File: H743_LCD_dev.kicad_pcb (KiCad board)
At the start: 2 copper layers, 39 parts, among them J1 BAT_SW, J2 TFT_LCD, J3 CAPACITIVE_CONTROLLER, SW1 SW_Push, U1 IS42S32800J-6TL, U2 STM32H743IITx

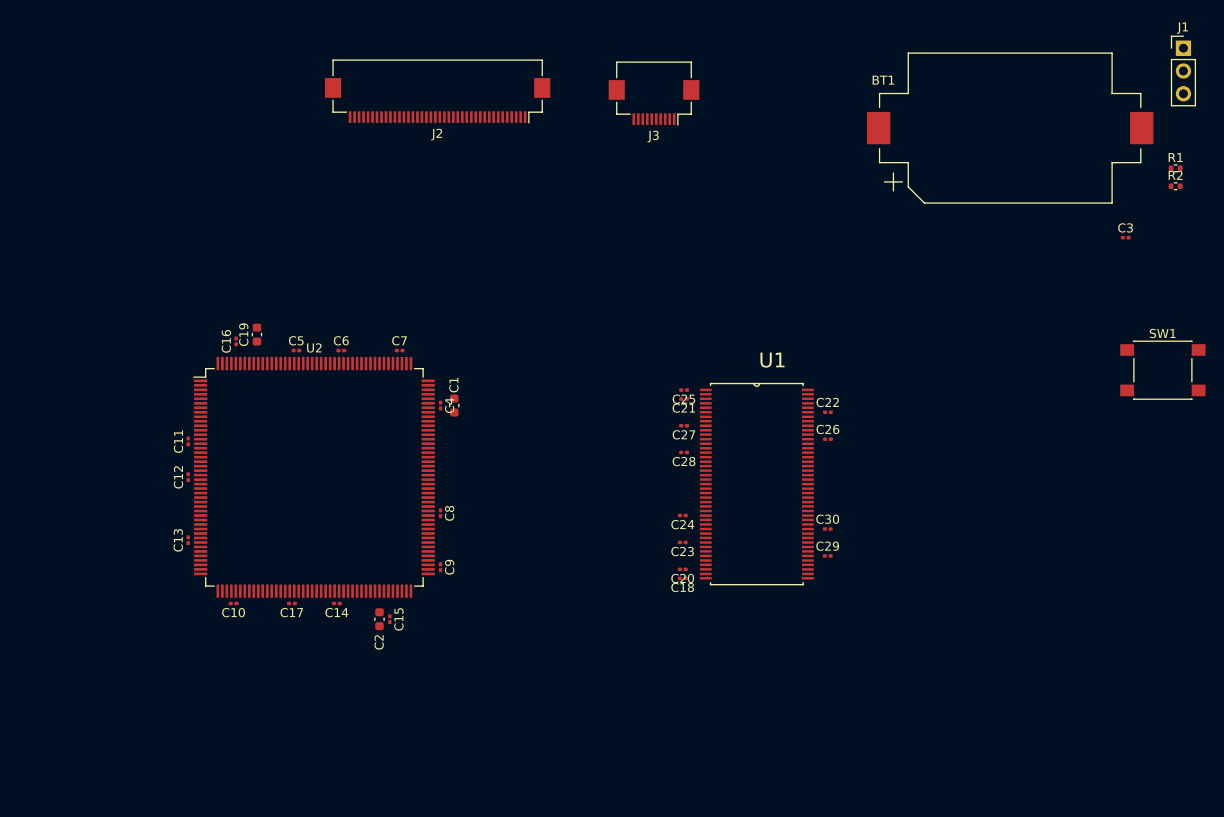
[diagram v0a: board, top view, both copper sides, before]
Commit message: Added UART, i2c, debug, NAND Flash, NOR Flash, EEPROM, SD-Card
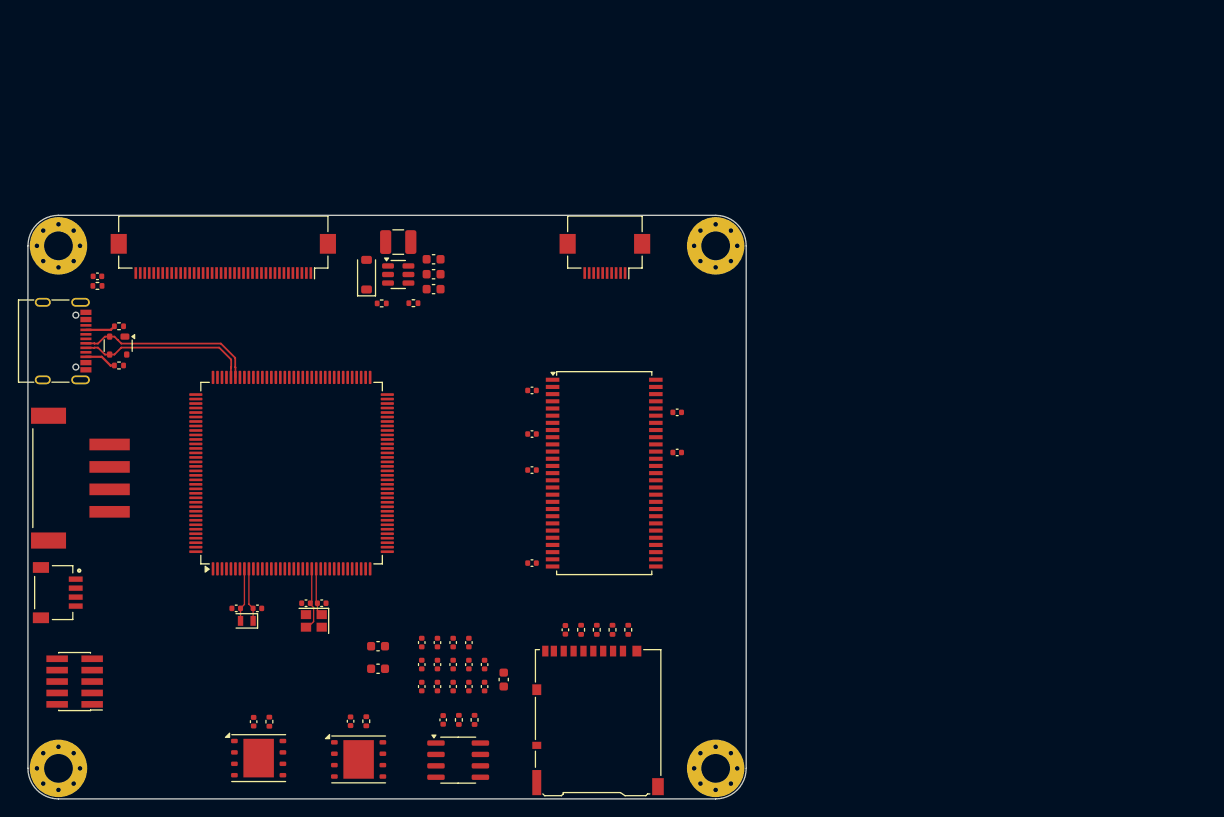
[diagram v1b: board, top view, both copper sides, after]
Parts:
- removed BT1: Battery_Cell, Battery:BatteryHolder_Keystone_1060_1x2032
- removed C23, C24, C25, C26, C27, C28, C29, C30: 100n, Capacitor_SMD:C_0201_0603Metric
- removed SW1: SW_Push, Button_Switch_SMD:SW_SPST_PTS645
- added C31: 1u, Capacitor_SMD:C_0603_1608Metric, F.Cu at (147.5, 74.8)
- added C32: 10u, Capacitor_SMD:C_0603_1608Metric, F.Cu at (147.5, 76.4)
- added C33: 10u, Capacitor_SMD:C_0603_1608Metric, F.Cu at (147.5, 78.1)
- added C34: 2u2, Capacitor_SMD:C_0603_1608Metric, F.Cu at (141.4, 117.9)
- added C35: 2u2, Capacitor_SMD:C_0603_1608Metric, F.Cu at (141.4, 120.4)
- added C36: 100n, Capacitor_SMD:C_0402_1005Metric, F.Cu at (158.5, 89.4)
- added C37: 100n, Capacitor_SMD:C_0402_1005Metric, F.Cu at (174.7, 96.3)
- added C38: 100n, Capacitor_SMD:C_0402_1005Metric, F.Cu at (174.7, 91.8)
- added C39: 10p, Capacitor_SMD:C_0402_1005Metric, F.Cu at (133.3, 113.1)
- added C40: 10p, Capacitor_SMD:C_0402_1005Metric, F.Cu at (135.1, 113.1)
- added C41: 22p, Capacitor_SMD:C_0402_1005Metric, F.Cu at (127.9, 113.7)
- added C42: 22p, Capacitor_SMD:C_0402_1005Metric, F.Cu at (125.6, 113.7)
- added C43: 4n7, Capacitor_SMD:C_0402_1005Metric, F.Cu at (110.1, 76.7)
- added D1: MSK4010, Diode_SMD:D_SOD-123, F.Cu at (140.1, 76.5)
- added D2: PRTR5V0U2X, Package_TO_SOT_SMD:SOT-143, F.Cu at (112.4, 84.4)
- added H1: MountingHole_Pad, MountingHole:MountingHole_3.2mm_M3_Pad_Via, F.Cu at (179.0, 131.5)
- added H2: MountingHole_Pad, MountingHole:MountingHole_3.2mm_M3_Pad_Via, F.Cu at (105.8, 131.5)
- added H3: MountingHole_Pad, MountingHole:MountingHole_3.2mm_M3_Pad_Via, F.Cu at (105.8, 73.3)
- added H4: MountingHole_Pad, MountingHole:MountingHole_3.2mm_M3_Pad_Via, F.Cu at (179.0, 73.3)
- added J4: USB-C, Connector_USB:USB_C_Receptacle_G-Switch_GT-USB-7010ASV, F.Cu at (105.1, 83.9)
- added J5: I2C-STEMMA-QT, SM04B-SRSS-TB_LF__SN_:JST_SM04B-SRSS-TB_LF__SN_, F.Cu at (107.7, 111.9)
- added J6: UART, KiCad:S4BXHSM4TBLFSN, F.Cu at (107.2, 99.2)
- added J7: Conn_02x05_Odd_Even, Connector_PinHeader_1.27mm:PinHeader_2x05_P1.27mm_Vertical_SMD, F.Cu at (107.6, 121.8)
- added L1: 10uH, Inductor_SMD:L_1210_3225Metric, F.Cu at (143.6, 72.9)
- added R10: 10K, Resistor_SMD:R_0402_1005Metric, F.Cu at (169.2, 116.1)
- added R11: 5K1, Resistor_SMD:R_0402_1005Metric, F.Cu at (112.5, 82.2)
- added R12: 5K1, Resistor_SMD:R_0402_1005Metric, F.Cu at (112.5, 86.6)
- added R13: 1M, Resistor_SMD:R_0402_1005Metric, F.Cu at (110.1, 77.7)
- added R3: 2.74R, Resistor_SMD:R_0402_1005Metric, F.Cu at (141.8, 79.7)
- added R4: 5K1, Resistor_SMD:R_0402_1005Metric, F.Cu at (145.3, 79.7)
- added R5: 2K2, Resistor_SMD:R_0402_1005Metric, F.Cu at (150.4, 126.1)
- added R6: 2K2, Resistor_SMD:R_0402_1005Metric, F.Cu at (152.1, 126.1)
- added R7: 10K, Resistor_SMD:R_0402_1005Metric, F.Cu at (164.0, 116.1)
- added R8: 10K, Resistor_SMD:R_0402_1005Metric, F.Cu at (165.7, 116.1)
- added R9: 10K, Resistor_SMD:R_0402_1005Metric, F.Cu at (167.5, 116.1)
- added U3: MT9284, Package_TO_SOT_SMD:SOT-23-6, F.Cu at (143.6, 76.5)
- added U4: STM32H723ZGTx, Package_QFP:LQFP-144_20x20mm_P0.5mm, F.Cu at (131.7, 98.6)
- added U5: W25N01GVZEIG, Package_SON:WSON-8-1EP_6x5mm_P1.27mm_EP3.4x4.3mm, F.Cu at (139.2, 130.5)
- added U7: CAT24C128, Package_SO:SOIC-8_3.9x4.9mm_P1.27mm, F.Cu at (150.3, 130.6)
- added Y1: 25MHz, Crystal:Crystal_SMD_2520-4Pin_2.5x2.0mm, F.Cu at (134.2, 115.1)
- added Y2: 32.768KHz, Crystal:Crystal_SMD_2012-2Pin_2.0x1.2mm, F.Cu at (126.7, 115.1)
- C1, C2: value 2u2 -> 100n; footprint Capacitor_SMD:C_0603_1608Metric -> Capacitor_SMD:C_0402_1005Metric
- C10, C11, C12, C13, C14, C15, C16, C17, C18, C20, C21, C22, C3, C4, C5, C6, C7, C8, C9: footprint Capacitor_SMD:C_0201_0603Metric -> Capacitor_SMD:C_0402_1005Metric
- J1: value BAT_SW -> Micro_SD_Card_Det_Hirose_DM3AT; footprint Connector_PinHeader_2.54mm:PinHeader_1x03_P2.54mm_Vertical -> Connector_Card:microSD_HC_Hirose_DM3AT-SF-PEJM5
- U1: value IS42S32800J-6TL -> W25Q128JVS; footprint IS42S32800J-6TL:SOP50P1176X120-86N -> Package_SON:WSON-8-1EP_6x5mm_P1.27mm_EP3.4x4.3mm
- U2: value STM32H743IITx -> IS42S16160J-7TL; footprint Package_QFP:LQFP-176_24x24mm_P0.5mm -> Package_SO:TSOP-II-54_22.2x10.16mm_P0.8mm
- moved R2 117.2 mm to (129.3, 126.3), turned to 90 degrees
- moved R1 109.2 mm to (140.1, 126.2), turned to 90 degrees
- moved J1 99.3 mm to (165.9, 126.1)
- moved C3 69.6 mm to (158.5, 94.2), turned to 180 degrees
- moved C22 63.3 mm to (138.3, 126.2), turned to 90 degrees
- moved U1 63.3 mm to (128.1, 130.3)
- moved C21 59.9 mm to (127.5, 126.3), turned to 90 degrees
- moved C19 47.2 mm to (155.4, 121.6)
- moved C16 41.4 mm to (149.7, 117.5)
- moved C5 40.6 mm to (148.0, 122.4), turned to 90 degrees
- moved C6 39.4 mm to (149.7, 122.4), turned to 90 degrees
- moved C11 38.6 mm to (149.7, 119.9)
- moved C7 38.2 mm to (151.5, 122.4), turned to 90 degrees
- moved C12 37.6 mm to (151.5, 119.9)
- moved C13 35.8 mm to (153.2, 119.9), turned to 90 degrees
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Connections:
- net /MEMORY/D0 renamed /MEMORY/NOR_DO(IO1)
- net /MEMORY/D2 renamed /MEMORY/NOR_DI(IO0)
- net /MEMORY/D3 renamed /MEMORY/NOR_IO3
- C1 pad 1: Net-(C1-Pad1) -> +3V3
- C10 pad 1: VDD -> +3V3
- C11 pad 1: VDD -> +3V3
- C12 pad 1: VDD -> +3V3
- C13 pad 1: VDD -> +3V3
- C14 pad 1: VDD -> +3V3
- C15 pad 1: VDD -> +3V3
- C16 pad 1: VDD -> +3V3
- C17 pad 1: VDD -> +3V3
- C19 pad 1: VDD -> +3V3
- C2 pad 1: Net-(C2-Pad1) -> +3V3
- C3 pad 1: GND -> +3V3
- C3 pad 2: /MCU/RST -> GND
- C4 pad 1: VDD -> +3V3
- C5 pad 1: VDD -> +3V3
- C6 pad 1: VDD -> +3V3
- C7 pad 1: VDD -> +3V3
- C8 pad 1: VDD -> +3V3
- C9 pad 1: VDD -> +3V3
- J1 pad 1: +3V3 -> /MEMORY/SD_DAT2
- J1 pad 2: Net-(J1-Pin_2) -> /MEMORY/SD_DAT3/CD
- J1 pad 3: Net-(BT1-+) -> /MEMORY/SD_CMD
- J2 pad 1: unconnected-(J2-Pad1) -> /LCD/LED_K
- J2 pad 10: unconnected-(J2-Pad10) -> /LCD/LCD_R5
- J2 pad 11: unconnected-(J2-Pad11) -> /LCD/LCD_R6
- J2 pad 12: unconnected-(J2-Pad12) -> /LCD/LCD_R7
- J2 pad 13: unconnected-(J2-Pad13) -> /LCD/LCD_G0
- J2 pad 14: unconnected-(J2-Pad14) -> /LCD/LCD_G1
- J2 pad 15: unconnected-(J2-Pad15) -> /LCD/LCD_G2
- J2 pad 16: unconnected-(J2-Pad16) -> /LCD/LCD_G3
- J2 pad 17: unconnected-(J2-Pad17) -> /LCD/LCD_G4
- J2 pad 18: unconnected-(J2-Pad18) -> /LCD/LCD_G5
- J2 pad 19: unconnected-(J2-Pad19) -> /LCD/LCD_G6
- J2 pad 2: unconnected-(J2-Pad2) -> /LCD/LED_A
- J2 pad 20: unconnected-(J2-Pad20) -> /LCD/LCD_G7
- J2 pad 21: unconnected-(J2-Pad21) -> /LCD/LCD_B0
- J2 pad 22: unconnected-(J2-Pad22) -> /LCD/LCD_B1
- J2 pad 23: unconnected-(J2-Pad23) -> /LCD/LCD_B2
- J2 pad 24: unconnected-(J2-Pad24) -> /LCD/LCD_B3
- J2 pad 25: unconnected-(J2-Pad25) -> /LCD/LCD_B4
- J2 pad 26: unconnected-(J2-Pad26) -> /LCD/LCD_B5
- J2 pad 27: unconnected-(J2-Pad27) -> /LCD/LCD_B6
- J2 pad 28: unconnected-(J2-Pad28) -> /LCD/LCD_B7
- J2 pad 29: unconnected-(J2-Pad29) -> GND
- J2 pad 30: unconnected-(J2-Pad30) -> /LCD/LCD_CLK
- J2 pad 31: unconnected-(J2-Pad31) -> /LCD/LCD_DISP
- J2 pad 32: unconnected-(J2-Pad32) -> /LCD/HSYNC
- J2 pad 33: unconnected-(J2-Pad33) -> /LCD/VSYNC
- J2 pad 34: unconnected-(J2-Pad34) -> /LCD/LCD_DE
- J2 pad 36: unconnected-(J2-Pad36) -> GND
- J2 pad 37: unconnected-(J2-Pad37) -> /LCD/XR
- J2 pad 38: unconnected-(J2-Pad38) -> /LCD/YD
- J2 pad 39: unconnected-(J2-Pad39) -> /LCD/XL
- J2 pad 4: unconnected-(J2-Pad4) -> VDD
- J2 pad 40: unconnected-(J2-Pad40) -> /LCD/YU
- J2 pad 5: unconnected-(J2-Pad5) -> /LCD/LCD_R0
- J2 pad 6: unconnected-(J2-Pad6) -> /LCD/LCD_R1
- J2 pad 7: unconnected-(J2-Pad7) -> /LCD/LCD_R2
- J2 pad 8: unconnected-(J2-Pad8) -> /LCD/LCD_R3
- J2 pad 9: unconnected-(J2-Pad9) -> /LCD/LCD_R4
- J2 pad MP: unconnected-(J2-MOUNT-PadMP) -> GND
- J3 pad 1: unconnected-(J3-Pad1) -> GND
- J3 pad 10: unconnected-(J3-Pad10) -> GND
- J3 pad 2: unconnected-(J3-Pad2) -> VDD
- J3 pad 3: unconnected-(J3-Pad3) -> /LCD/LCD_SCL
- J3 pad 4: unconnected-(J3-Pad4) -> GND
- J3 pad 5: unconnected-(J3-Pad5) -> /LCD/LCD_SDA
- J3 pad 6: unconnected-(J3-Pad6) -> GND
- J3 pad 7: unconnected-(J3-Pad7) -> /LCD/~{LCD_RST}
- J3 pad 8: unconnected-(J3-Pad8) -> /LCD/LCD_WAKE
- J3 pad 9: unconnected-(J3-Pad9) -> /LCD/~{LCD_INT}
- J3 pad MP: unconnected-(J3-MOUNT-PadMP) -> GND
- R1 pad 1: VDD -> +3V3
- R1 pad 2: Net-(U2-PDR_ON) -> /MEMORY/~{NAND_CS}
- R2 pad 1: VDD -> +3V3
- R2 pad 2: /MCU/RST -> /MEMORY/~{NOR_CS}
- U1 pad 1: +3V3 -> /MEMORY/~{NOR_CS}
- U1 pad 3: +3V3 -> /MEMORY/NOR_IO2
- U1 pad 4: /MEMORY/D1 -> GND
- U1 pad 6: GND -> /MEMORY/NOR_CLK
- U1 pad 8: /MEMORY/D4 -> +3V3
- U1 pad 9: +3V3 -> GND
- U2 pad 1: /MCU/PE2 -> +3V3
- U2 pad 10: /MCU/PC15 -> /MCU/DQ5
- U2 pad 11: /MCU/PI9 -> /MCU/DQ6
- U2 pad 12: /MCU/PI10 -> GND
- U2 pad 13: /MCU/PI11 -> /MCU/DQ7
- U2 pad 14: GND -> +3V3
- U2 pad 15: VDD -> /MCU/PE0
- U2 pad 16: /MCU/PF0 -> /MCU/PC0
- U2 pad 17: /MCU/PF1 -> /MCU/PG15
- U2 pad 18: /MCU/PF2 -> /MCU/PF11
- U2 pad 19: /MCU/PF3 -> /MCU/PC4
- U2 pad 2: /MCU/PE3 -> /MCU/DQ0
- U2 pad 20: /MCU/PF4 -> /MCU/PG4
- U2 pad 21: /MCU/PF5 -> /MCU/PG5
- U2 pad 22: GND -> /MCU/A10
- U2 pad 23: VDD -> /MCU/A0
- U2 pad 24: /MCU/PF6 -> /MCU/A1
- U2 pad 25: /MCU/PF7 -> /MCU/A2
- U2 pad 26: /MCU/PF8 -> /MCU/A3
- U2 pad 27: /MCU/PF9 -> +3V3
- U2 pad 28: /MCU/PF10 -> GND
- U2 pad 29: /MCU/PH0 -> /MCU/A4
- U2 pad 3: /MCU/PE4 -> +3V3
- U2 pad 30: /MCU/PH1 -> /MCU/A5
- U2 pad 31: /MCU/RST -> /MCU/A6
- U2 pad 32: /MCU/PC0 -> /MCU/A7
- U2 pad 33: /MCU/PC1 -> /MCU/A8
- U2 pad 34: /MCU/PC2 -> /MCU/A9
- U2 pad 35: /MCU/PC3 -> /MCU/A11
- U2 pad 36: VDD -> unconnected-(U2-NC-Pad36)
- U2 pad 37: GND -> /MCU/PC5
- U2 pad 38: unconnected-(U2-VREF+-Pad38) -> /MCU/PG8
- U2 pad 39: /MCU/VDDA -> /MCU/PE1
- U2 pad 4: /MCU/PE5 -> /MCU/DQ1
- U2 pad 40: /MCU/PA0 -> unconnected-(U2-NC-Pad40)
- U2 pad 41: /MCU/PA1 -> GND
- U2 pad 42: /MCU/PA2 -> /MCU/DQ8
- U2 pad 43: /MCU/PH2 -> +3V3
- U2 pad 44: /MCU/PH3 -> /MCU/DQ9
- U2 pad 45: /MCU/PH4 -> /MCU/DQ10
- U2 pad 46: /MCU/PH5 -> GND
- U2 pad 47: /MCU/PA3 -> /MCU/DQ11
- U2 pad 48: GND -> /MCU/DQ12
- U2 pad 49: VDD -> +3V3
- U2 pad 5: /MCU/PE6 -> /MCU/DQ2
- U2 pad 50: /MCU/PA4 -> /MCU/DQ13
- U2 pad 51: /MCU/PA5 -> /MCU/DQ14
- U2 pad 52: /MCU/PA6 -> GND
- U2 pad 53: /MCU/PA7 -> /MCU/DQ15
- U2 pad 54: /MCU/PC4 -> GND
- U2 pad 6: Net-(J1-Pin_2) -> GND
- U2 pad 7: /MCU/PI8 -> /MCU/DQ3
- U2 pad 8: /MCU/PC13 -> /MCU/DQ4
- U2 pad 9: /MCU/PC14 -> +3V3
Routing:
- net /MCU/USB_D-: track 0.00 -> 20.1 mm
- net /MCU/USB_D+: track 0.00 -> 19.4 mm
- net /MCU/XIN: track 0.00 -> 7.20 mm
- net /MCU/OSC32_OUT: track 0.00 -> 5.99 mm
- net /MCU/OSC32_IN: track 0.00 -> 5.98 mm
- net /MCU/XOUT: track 0.00 -> 5.35 mm
- net Net-(J4-CC2): track 0.00 -> 3.57 mm
- net Net-(J4-CC1): track 0.00 -> 3.34 mm
- added copper zone on In1.Cu, net GND
- added copper zone on In4.Cu, net GND
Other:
- board outline added: 80 x 65 mm
- copper layers 2 -> 6

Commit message: Added I2S Audio amplifier
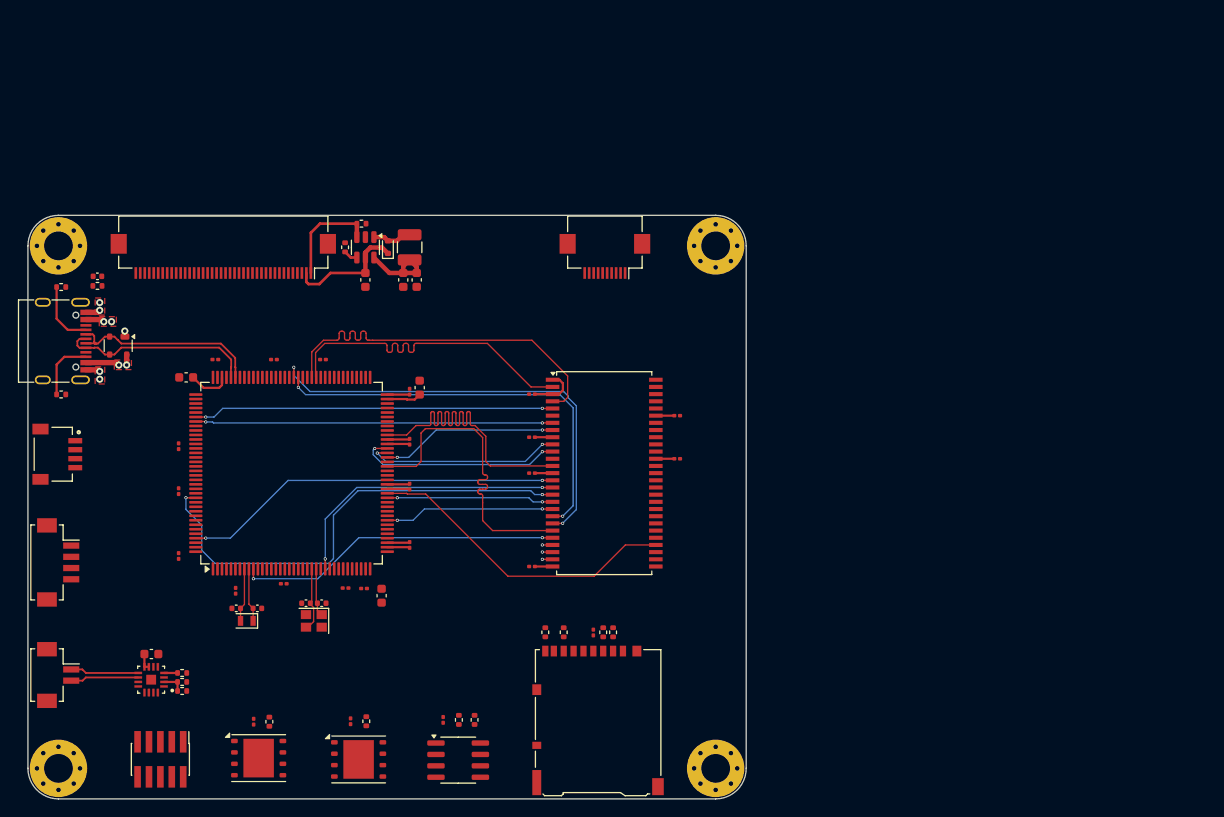
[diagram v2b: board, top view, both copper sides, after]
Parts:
- removed J6: UART, KiCad:S4BXHSM4TBLFSN
- added C23: 10u, Capacitor_SMD:C_0603_1608Metric, F.Cu at (116.1, 118.8)
- added J8: SPKR, Connector_Hirose:Hirose_DF13C_CL535-0402-2-51_1x02-1MP_P1.25mm_Vertical, F.Cu at (105.7, 121.1)
- added J9: UART, Connector_Hirose:Hirose_DF13C_CL535-0404-8-51_1x04-1MP_P1.25mm_Vertical, F.Cu at (105.7, 108.5)
- added R14: 1M, Resistor_SMD:R_0402_1005Metric, F.Cu at (119.5, 120.9)
- added R15: NC, Resistor_SMD:R_0402_1005Metric, F.Cu at (119.5, 121.9)
- added R16: NC, Resistor_SMD:R_0402_1005Metric, F.Cu at (119.5, 122.9)
- added U6: MAX98357AETE_, MAX98357AETE_:QFN50P300X300X80-17N, F.Cu at (116.1, 121.6)
- C1, C10, C11, C12, C13, C14, C15, C16, C17, C18, C2, C20, C21, C22, C3, C36, C37, C38, C4, C5, C6, C7, C8, C9: footprint Capacitor_SMD:C_0402_1005Metric -> Capacitor_SMD:C_0201_0603Metric
- D1: footprint Diode_SMD:D_SOD-123 -> Diode_SMD:D_SOD-523
- moved C7 46.1 mm to (123.2, 86.0), turned to 0 degrees
- moved C8 43.3 mm to (119.2, 95.6)
- moved C6 41.5 mm to (129.8, 86.0), turned to 0 degrees
- moved C13 39.2 mm to (119.2, 100.6)
- moved C35 38.9 mm to (120.0, 87.9), turned to 180 degrees
- moved C5 38.6 mm to (135.2, 86.0), turned to 0 degrees
- moved C12 34.5 mm to (119.2, 107.8), turned to -90 degrees
- moved C34 29.2 mm to (146.0, 89.1), turned to 90 degrees
- moved C17 28.7 mm to (144.9, 89.5)
- moved C11 25.6 mm to (125.5, 111.7), turned to -90 degrees
- moved C16 22.9 mm to (144.9, 95.1), turned to -90 degrees
- moved C10 19.3 mm to (130.9, 110.9), turned to 180 degrees
- moved C15 17.6 mm to (144.9, 100.1), turned to -90 degrees
- moved C19 16.5 mm to (141.8, 112.3), turned to -90 degrees
- moved J5 15.4 mm to (107.6, 96.5)
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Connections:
- D2 pad 4: unconnected-(D2-VCC-Pad4) -> VBUS
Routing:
- net /MCU/PG15: track 0.00 -> 53.7 mm, vias 0 -> 2
- net /MCU/PG5: track 0.00 -> 49.8 mm, vias 0 -> 2
- net /MCU/PG4: track 0.00 -> 46.3 mm, vias 0 -> 2
- net /MCU/DQ1: track 0.00 -> 42.4 mm
- net /MCU/PE0: track 0.00 -> 42.4 mm, vias 0 -> 2
- net /MCU/DQ2: track 0.00 -> 40.1 mm, vias 0 -> 2
- net /MCU/DQ3: track 0.00 -> 39.8 mm, vias 0 -> 2
- net /MCU/DQ7: track 0.00 -> 39.2 mm
- net /MCU/A0: track 0.00 -> 36.3 mm, vias 0 -> 2
- net /MCU/DQ0: track 0.00 -> 36.3 mm
- net /MCU/A10: track 0.00 -> 35.5 mm
- net /MCU/A6: track 0.00 -> 35.2 mm
- net /MCU/PC0: track 0.00 -> 32.3 mm, vias 0 -> 2
- net +3V3: track 0.00 -> 25.5 mm
- net /MCU/DQ6: track 0.00 -> 23.2 mm, vias 0 -> 2
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- added copper zone on F.Cu, net GND
- added copper zone on F.Cu, net VBUS

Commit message: Add net class, not clear yet
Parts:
- moved C5 0.07 mm to (135.3, 86.0)
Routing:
- net /MCU/PG8: track 0.00 -> 54.2 mm
- net /MCU/PE1: track 0.00 -> 53.5 mm
- net /MCU/PG15: track 53.7 -> 10.6 mm, vias 2 -> 0
- net /MCU/PG5: track 49.8 -> 12.7 mm, vias 2 -> 0
- net /MCU/PG4: track 46.3 -> 13.4 mm, vias 2 -> 0
- net /MCU/PE0: track 42.4 -> 11.3 mm, vias 2 -> 0
- net /MCU/DQ7: track 39.2 -> 11.1 mm
- net /MCU/DQ2: track 40.1 -> 12.2 mm, vias 2 -> 0
- net /MCU/DQ3: track 39.8 -> 12.2 mm, vias 2 -> 0
- net /MCU/A4: track 0.00 -> 26.9 mm
- net /MCU/A5: track 0.00 -> 26.8 mm
- net /MCU/A7: track 0.00 -> 25.1 mm
- net /MCU/A8: track 0.00 -> 24.3 mm
- net /MCU/A0: track 36.3 -> 12.3 mm, vias 2 -> 0
- net /MCU/A10: track 35.5 -> 12.5 mm
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
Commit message: Edited PCB
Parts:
- moved C36 4.33 mm to (154.2, 89.6)
- moved C1 4.33 mm to (154.2, 108.8)
- moved C2 4.33 mm to (154.2, 98.4)
- moved C3 4.33 mm to (154.2, 94.4)
- moved C37 4.33 mm to (170.4, 96.8)
- moved C38 4.33 mm to (170.4, 92.0)
- moved U2 4.32 mm to (162.2, 98.6)
- moved C10 0.81 mm to (131.5, 111.5)
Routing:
- net /MCU/DQ15: track 7.60 -> 54.6 mm
- net /MCU/DQ14: track 10.8 -> 54.5 mm
- net /MCU/DQ13: track 12.3 -> 55.7 mm
- net /MCU/A3: track 11.6 -> 52.8 mm, vias 0 -> 2
- net /MCU/DQ7: track 11.1 -> 52.1 mm, vias 0 -> 2
- net /MCU/A0: track 12.3 -> 52.0 mm, vias 0 -> 2
- net /MCU/A1: track 12.1 -> 51.8 mm, vias 0 -> 2
- net /MCU/A2: track 11.7 -> 51.3 mm, vias 0 -> 2
- net /MCU/PC4: track 18.9 -> 52.6 mm, vias 0 -> 2
- net /MCU/A11: track 21.7 -> 55.3 mm
- net /MCU/A9: track 22.7 -> 54.2 mm
- net /MCU/A8: track 24.3 -> 55.6 mm
- net /MCU/PC5: track 21.1 -> 51.7 mm, vias 0 -> 2
- net /MCU/PE0: track 11.3 -> 38.1 mm, vias 0 -> 2
- net /MCU/A5: track 26.8 -> 52.3 mm, vias 0 -> 2
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
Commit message: WIP
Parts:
- moved C1 19.6 mm to (173.7, 106.6), turned to -90 degrees
- moved C36 17.0 mm to (154.5, 106.6), turned to -90 degrees
- moved C38 13.6 mm to (156.9, 90.4), turned to 90 degrees
- moved C3 13.2 mm to (159.3, 106.6), turned to -90 degrees
- moved C2 12.3 mm to (163.3, 106.6), turned to -90 degrees
- moved C37 10.7 mm to (161.7, 90.4), turned to 90 degrees
- moved U2 1.07 mm to (163.3, 98.6), turned to 90 degrees
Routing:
- net /MCU/PG4: track 1.13 -> 66.9 mm, vias 1 -> 2
- net /MCU/PG5: track 1.79 -> 66.9 mm, vias 1 -> 2
- net /MCU/PG15: track 1.79 -> 66.9 mm, vias 1 -> 2
- net /MCU/DQ3: track 10.2 -> 66.9 mm, vias 1 -> 2
- net /MCU/DQ2: track 10.6 -> 66.9 mm, vias 1 -> 2
- net /MCU/DQ0: track 24.1 -> 66.9 mm
- net /MCU/DQ1: track 24.5 -> 66.9 mm
- net /MCU/A10: track 1.13 -> 42.0 mm, vias 1 -> 2
- net /MCU/PC0: track 1.13 -> 32.7 mm, vias 1 -> 2
- net /MCU/DQ15: track 54.6 -> 27.0 mm
- net /MCU/DQ13: track 55.7 -> 28.4 mm
- net /MCU/PF11: track 52.9 -> 25.9 mm, vias 2 -> 0
- net /MCU/DQ14: track 54.5 -> 28.0 mm
- net /MCU/DQ7: track 52.1 -> 25.9 mm
- net /MCU/PC4: track 52.6 -> 26.7 mm
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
